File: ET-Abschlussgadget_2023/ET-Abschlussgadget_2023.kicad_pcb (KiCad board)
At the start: 2 copper layers, 85 x 54 mm, 0 parts

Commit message: Added first & last name
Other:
- board text added: "char firstName[] = {dblquote} {dblquote};"
- board text added: "char lastName[] = {dblquote} {dblquote};"
- board text added: "uint16_t avgAge = 25;"
- board text removed: "char first[] = {dblquote}PREN{dblquote};"
- board text removed: "char last[] = {dblquote}Punkt{dblquote};"
- board text removed: "uint16_t age = 1997;"
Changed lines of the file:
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@@
   (gr_line (start 113.625 95) (end 115.875 95)
     (stroke (width 0.15) (type default)) (layer "F.SilkS"))
+  (gr_poly
+    (pts
+      (xy 136.3 109)
+      (xy 165.1 109)
+      (xy 165.1 112)
+      (xy 136.3 112)
+    )
+    (stroke (width 0.15) (type solid)) (fill solid) (layer "F.SilkS"))
+  (gr_poly
+    (pts
+      (xy 135.8 101)
+      (xy 164.6 101)
+      (xy 164.6 104)
+      (xy 135.8 104)
+    )
+    (stroke (width 0.15) (type solid)) (fill solid) (layer "F.SilkS"))
   (gr_line (start 116.175 88.525) (end 114.925 88.525)
     (stroke (width 0.15) (type default)) (layer "F.SilkS"))
@@
     )
   )
-  (gr_text "uint16_t age = 1997;" (at 104 120) (layer "F.SilkS")
+  (gr_text "uint16_t avgAge = 25;" (at 104 120) (layer "F.SilkS")
     (effects (font (size 2 2) (thickness 0.3)) (justify left bottom))
   )
-  (gr_text "char last[] = {dblquote}Punkt{dblquote};" (at 104 104) (layer "F.SilkS")
+  (gr_text "char lastName[] = {dblquote}                   {dblquote};" (at 104 104) (layer "F.SilkS")
     (effects (font (size 2 2) (thickness 0.3)) (justify left bottom))
   )
@@
     (effects (font (size 1 1) (thickness 0.2) bold) (justify left bottom))
   )
-  (gr_text "char first[] = {dblquote}PREN{dblquote};" (at 104 112) (layer "F.SilkS")
+  (gr_text "char firstName[] = {dblquote}                   {dblquote};" (at 104 112) (layer "F.SilkS")
     (effects (font (size 2 2) (thickness 0.3)) (justify left bottom))
   )

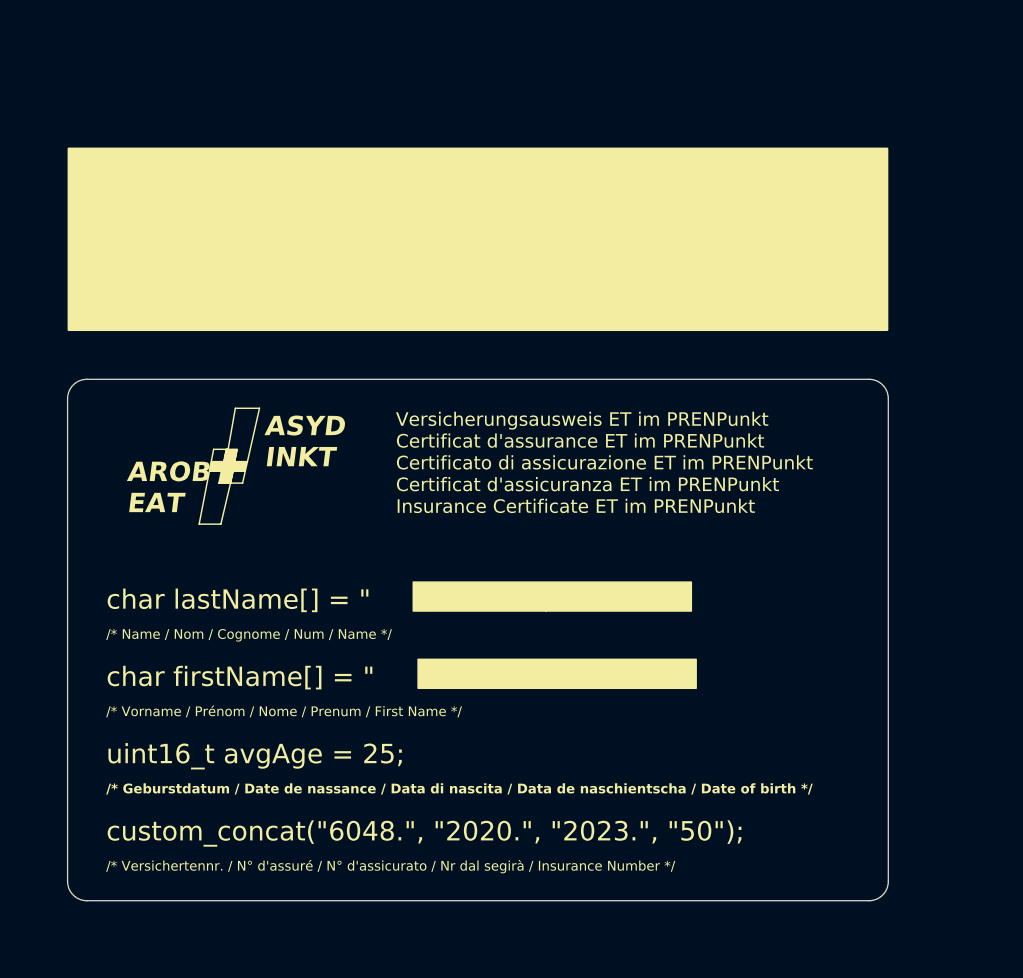
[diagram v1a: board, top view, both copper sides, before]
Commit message: Add basic layout
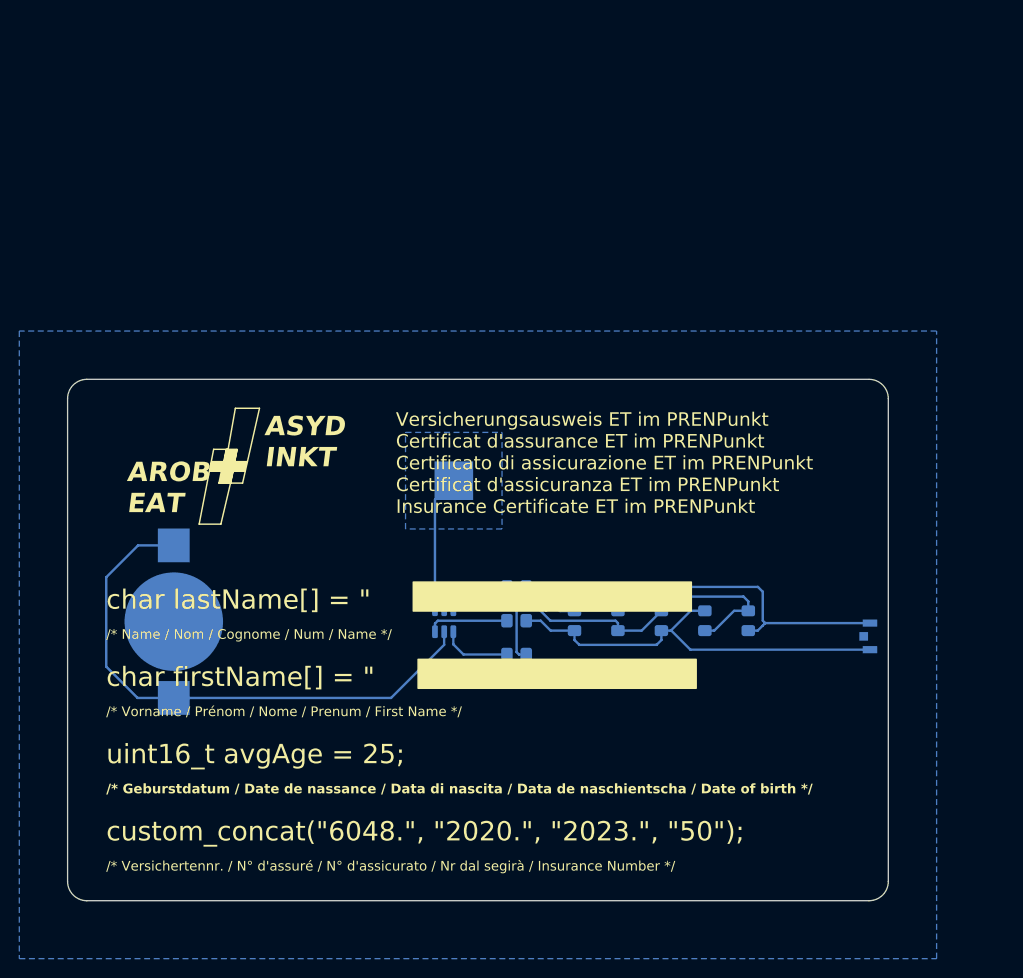
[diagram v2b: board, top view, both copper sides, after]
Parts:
- added BT1: 3V, Battery:BatteryHolder_Keystone_3000_1x12mm, B.Cu at (111.0, 105.1)
- added D1: LED_Red, LED_SMD:LED_0805_2012Metric_Pad1.15x1.40mm_HandSolder, B.Cu at (170.5, 105.0)
- added D2: LED_Red, LED_SMD:LED_0805_2012Metric_Pad1.15x1.40mm_HandSolder, B.Cu at (166.0, 105.0)
- added D3: LED_Red, LED_SMD:LED_0805_2012Metric_Pad1.15x1.40mm_HandSolder, B.Cu at (157.0, 105.0)
- added D4: LED_Red, LED_SMD:LED_0805_2012Metric_Pad1.15x1.40mm_HandSolder, B.Cu at (161.5, 105.0)
- added D5: LED_Red, LED_SMD:LED_0805_2012Metric_Pad1.15x1.40mm_HandSolder, B.Cu at (152.5, 105.0)
- added D6: LED_Ir, LED_SMD:LED_LiteOn_LTST-S326, B.Cu at (183.1, 106.6)
- added R1: 220R, Resistor_SMD:R_0805_2012Metric_Pad1.20x1.40mm_HandSolder, B.Cu at (146.5, 101.5)
- added R2: 220R, Resistor_SMD:R_0805_2012Metric_Pad1.20x1.40mm_HandSolder, B.Cu at (146.5, 108.5)
- added R3: 220R, Resistor_SMD:R_0805_2012Metric_Pad1.20x1.40mm_HandSolder, B.Cu at (146.5, 105.0)
- added TP1: Capacitive Pad, TestPoint:TestPoint_Pad_4.0x4.0mm, B.Cu at (140.0, 90.5)
- added U1: ATtiny10-TS, Package_TO_SOT_SMD:SOT-23-6, B.Cu at (139.0, 105.0)
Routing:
- net VCC: track 0.00 -> 57.6 mm
- net Net-(D1-K): track 0.00 -> 44.2 mm
- net Net-(D2-A): track 0.00 -> 43.6 mm
- net Net-(D1-A): track 0.00 -> 39.8 mm
- net /Cap_Pad: track 0.00 -> 14.2 mm
- net Net-(U1-~{RESET}/PB3): track 0.00 -> 8.41 mm
- net Net-(U1-PB2): track 0.00 -> 7.30 mm
- net Net-(U1-PB1): track 0.00 -> 7.30 mm
- added copper zone on B.Cu, net /Cap_Pad
- added copper zone on B.Cu, net GND

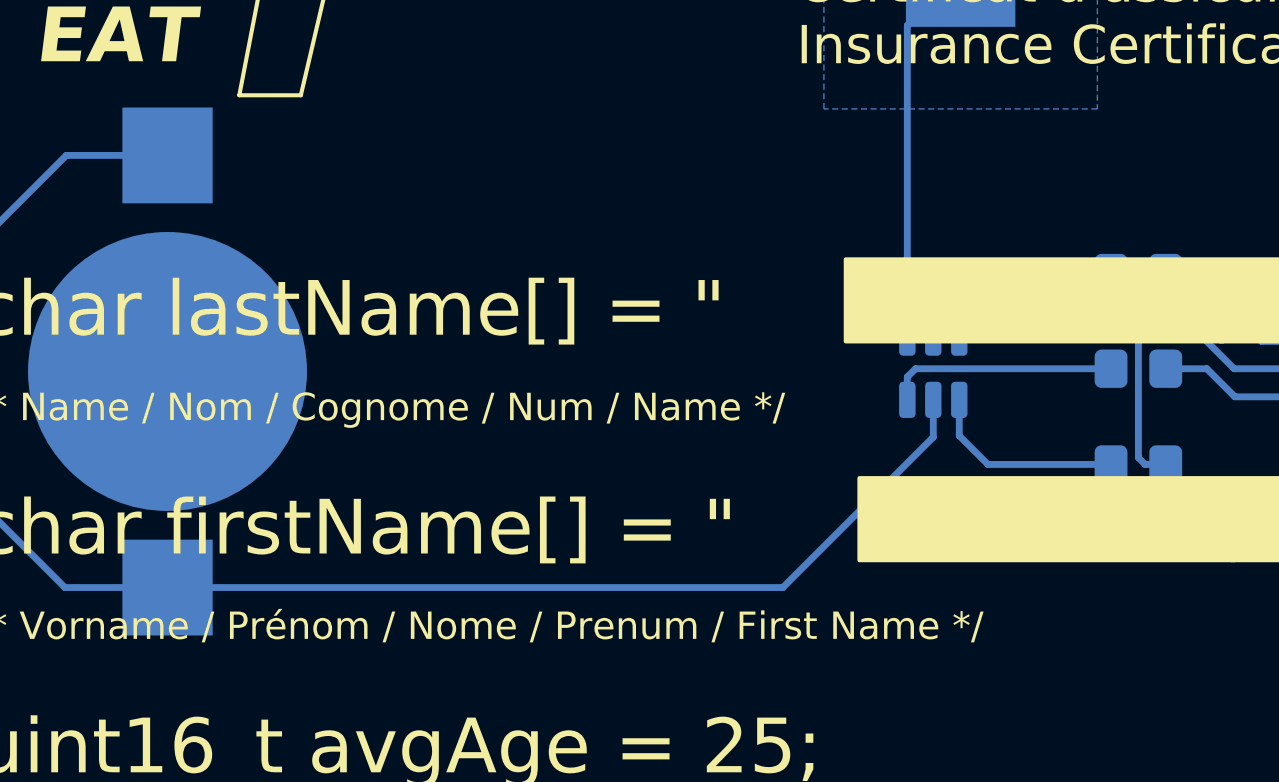
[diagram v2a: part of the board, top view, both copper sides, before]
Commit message: Add testpoints, bottom silkscreen, rothli
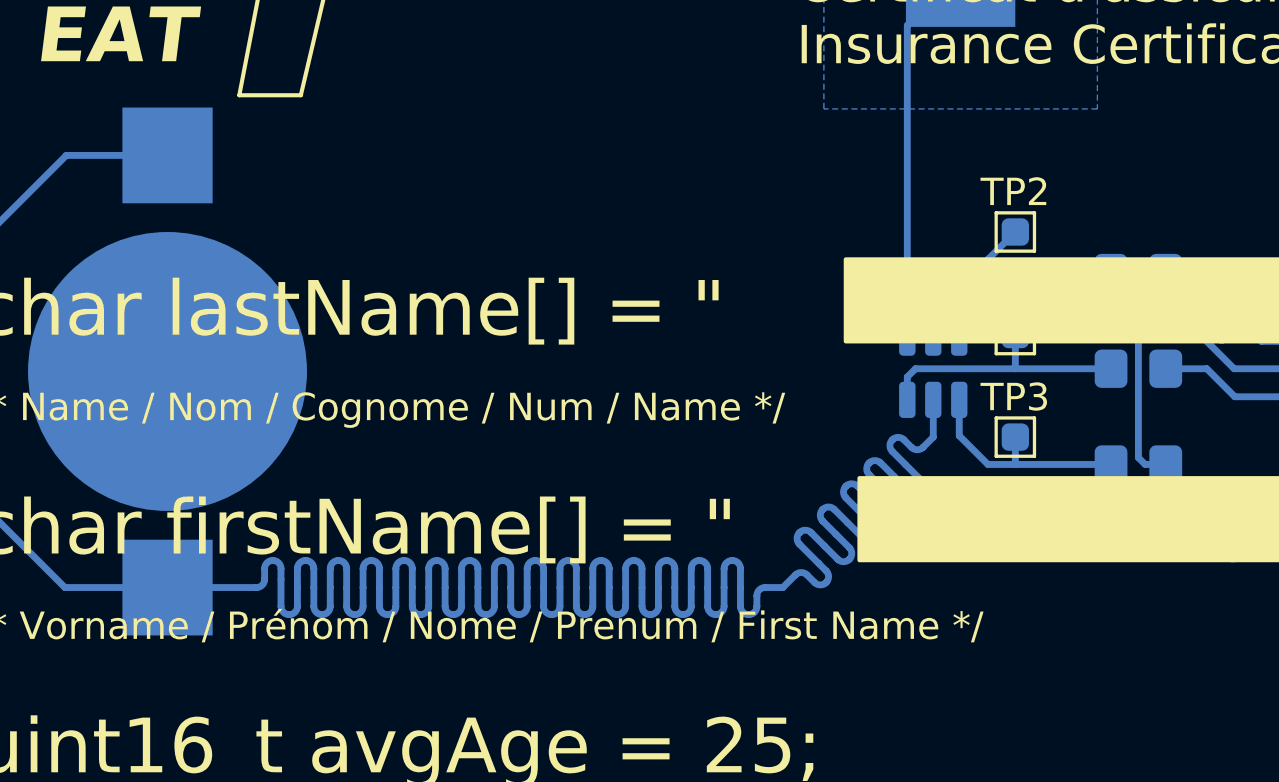
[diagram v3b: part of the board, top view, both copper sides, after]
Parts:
- added G***: LOGO, LOGO, B.Cu at (121.0, 124.0)
- added G***: LOGO, LOGO, B.Cu at (230.0, 118.0)
- added TP2: TestPoint, TestPoint:TestPoint_Pad_1.0x1.0mm, F.Cu at (142.0, 100.0)
- added TP3: TestPoint, TestPoint:TestPoint_Pad_1.0x1.0mm, F.Cu at (142.0, 107.5)
- added TP4: TestPoint, TestPoint:TestPoint_Pad_1.0x1.0mm, F.Cu at (142.0, 103.8)
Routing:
- net VCC: track 57.6 -> 125.0 mm
- net Net-(U1-PB1): track 7.30 -> 9.21 mm
- net Net-(U1-~{RESET}/PB3): track 8.41 -> 9.66 mm
- net Net-(U1-PB2): track 7.30 -> 8.30 mm
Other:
- board text added: "DE"
- board text added: "DRÜCK MICH!"
- board text added: "ET"
- board text added: "ET: Wie WI, nur besser"
- board text added: "MEDTECH"
- board text added: "MT"
- board text added: "WI"
- board text added: "WIE ASSI BIST DU?"

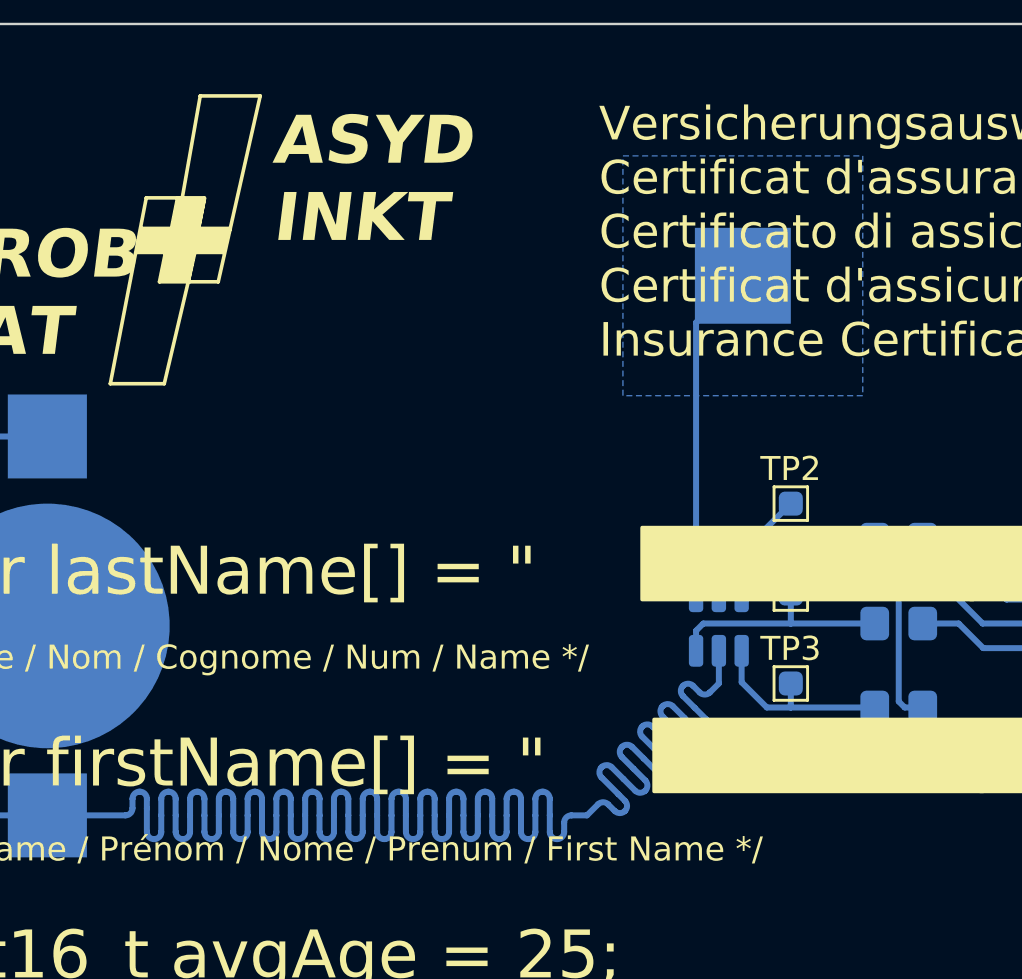
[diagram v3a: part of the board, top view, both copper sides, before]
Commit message: Fix silkscreen and solder mask
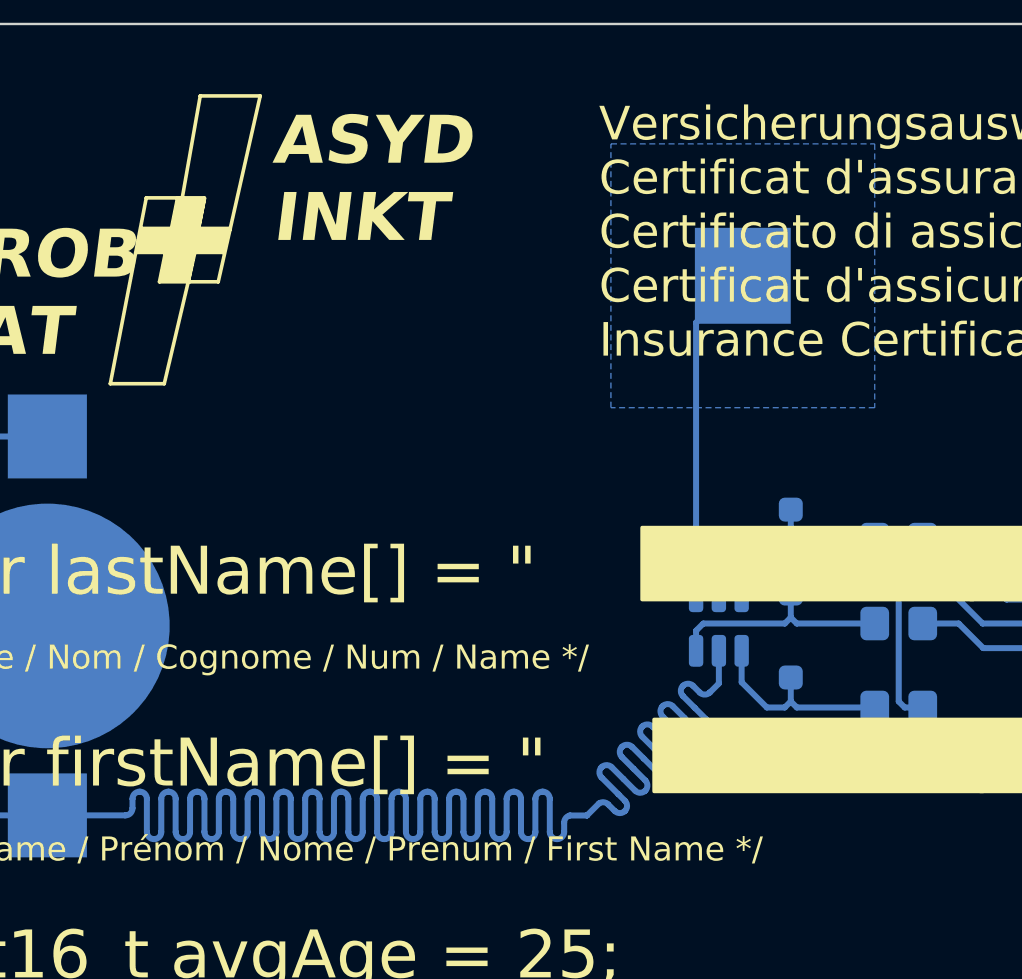
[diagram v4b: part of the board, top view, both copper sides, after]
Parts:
- TP2, TP3, TP4: moved to B.Cu
- moved TP2 0.25 mm to (142.0, 100.2), turned to 180 degrees
- moved TP3 0.25 mm to (142.0, 107.2), turned to 180 degrees
- turned TP4 to 180 degrees
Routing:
- net Net-(U1-PB1): track 9.21 -> 8.50 mm

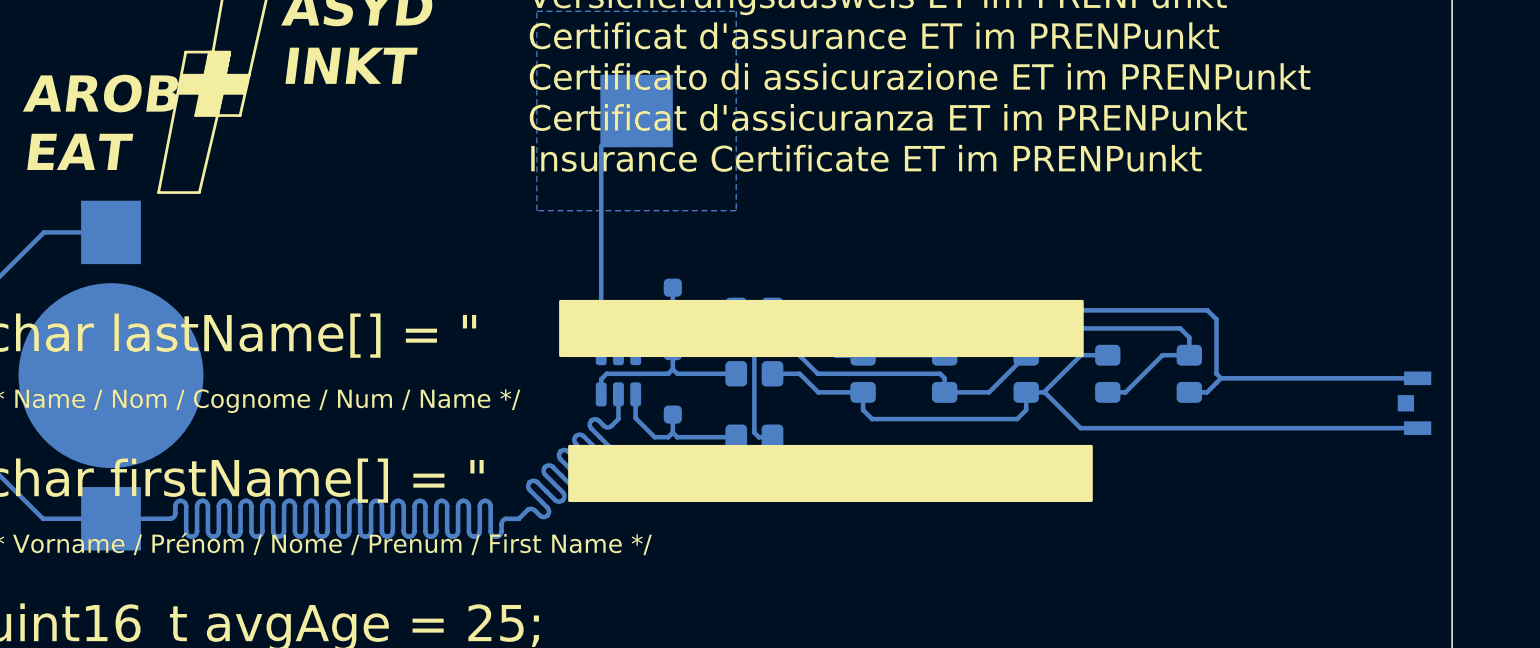
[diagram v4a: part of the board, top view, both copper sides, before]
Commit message: Improve component and silkscreen placement
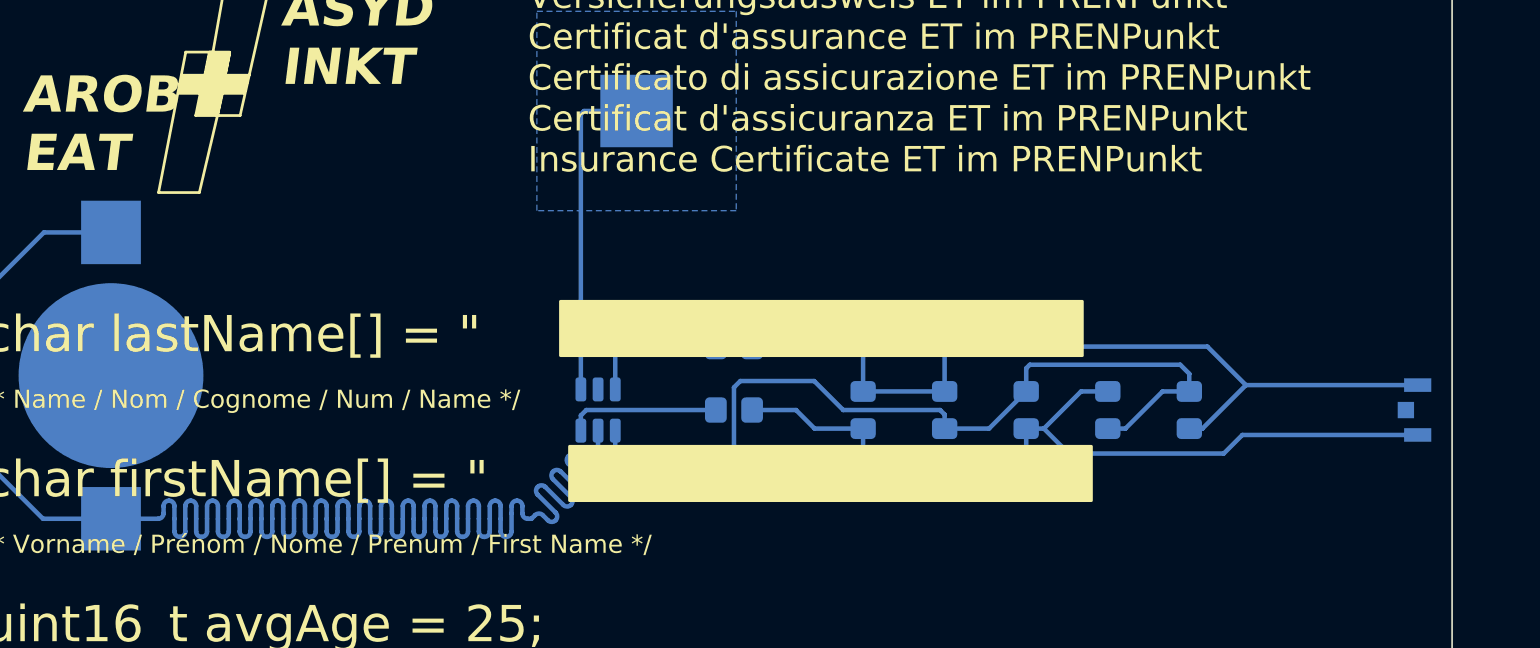
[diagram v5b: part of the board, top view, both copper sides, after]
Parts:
- removed TP2, TP3, TP4: TestPoint, TestPoint:TestPoint_Pad_1.0x1.0mm
- moved R1 2.29 mm to (145.4, 103.5)
- moved R2 2.29 mm to (145.4, 110.5)
- moved R3 2.29 mm to (145.4, 107.0)
- moved U1 2.29 mm to (137.9, 107.0)
- moved D1 2.00 mm to (170.5, 107.0)
- moved D2 2.00 mm to (166.0, 107.0)
- moved D3 2.00 mm to (161.5, 107.0)
- moved D4 2.00 mm to (157.0, 107.0)
- moved D5 2.00 mm to (152.5, 107.0)
- moved D6 0.38 mm to (183.1, 107.0)
- renumbered D4 to D3, D3 to D4
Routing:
- net /Cap_Pad: track 14.2 -> 18.3 mm
- net VCC: track 125.0 -> 122.0 mm
- net Net-(D1-K): track 44.2 -> 46.5 mm
- net Net-(D1-A): track 39.8 -> 41.2 mm
- net Net-(D2-A): track 43.6 -> 44.9 mm
- net Net-(U1-~{RESET}/PB3): track 9.62 -> 8.41 mm
- net Net-(U1-PB2): track 8.50 -> 7.75 mm
- net Net-(U1-PB1): track 8.50 -> 7.75 mm
